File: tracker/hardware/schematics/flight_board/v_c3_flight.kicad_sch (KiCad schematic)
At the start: 28 parts, among them J1 Prog_Header, J2 Debug_Header, U1 ESP32-C3-WROOM-02, U2 LoRa2021_Gen4, U3 MAX-M10S, U4 TPS7A02, U5 MS5611-01BA

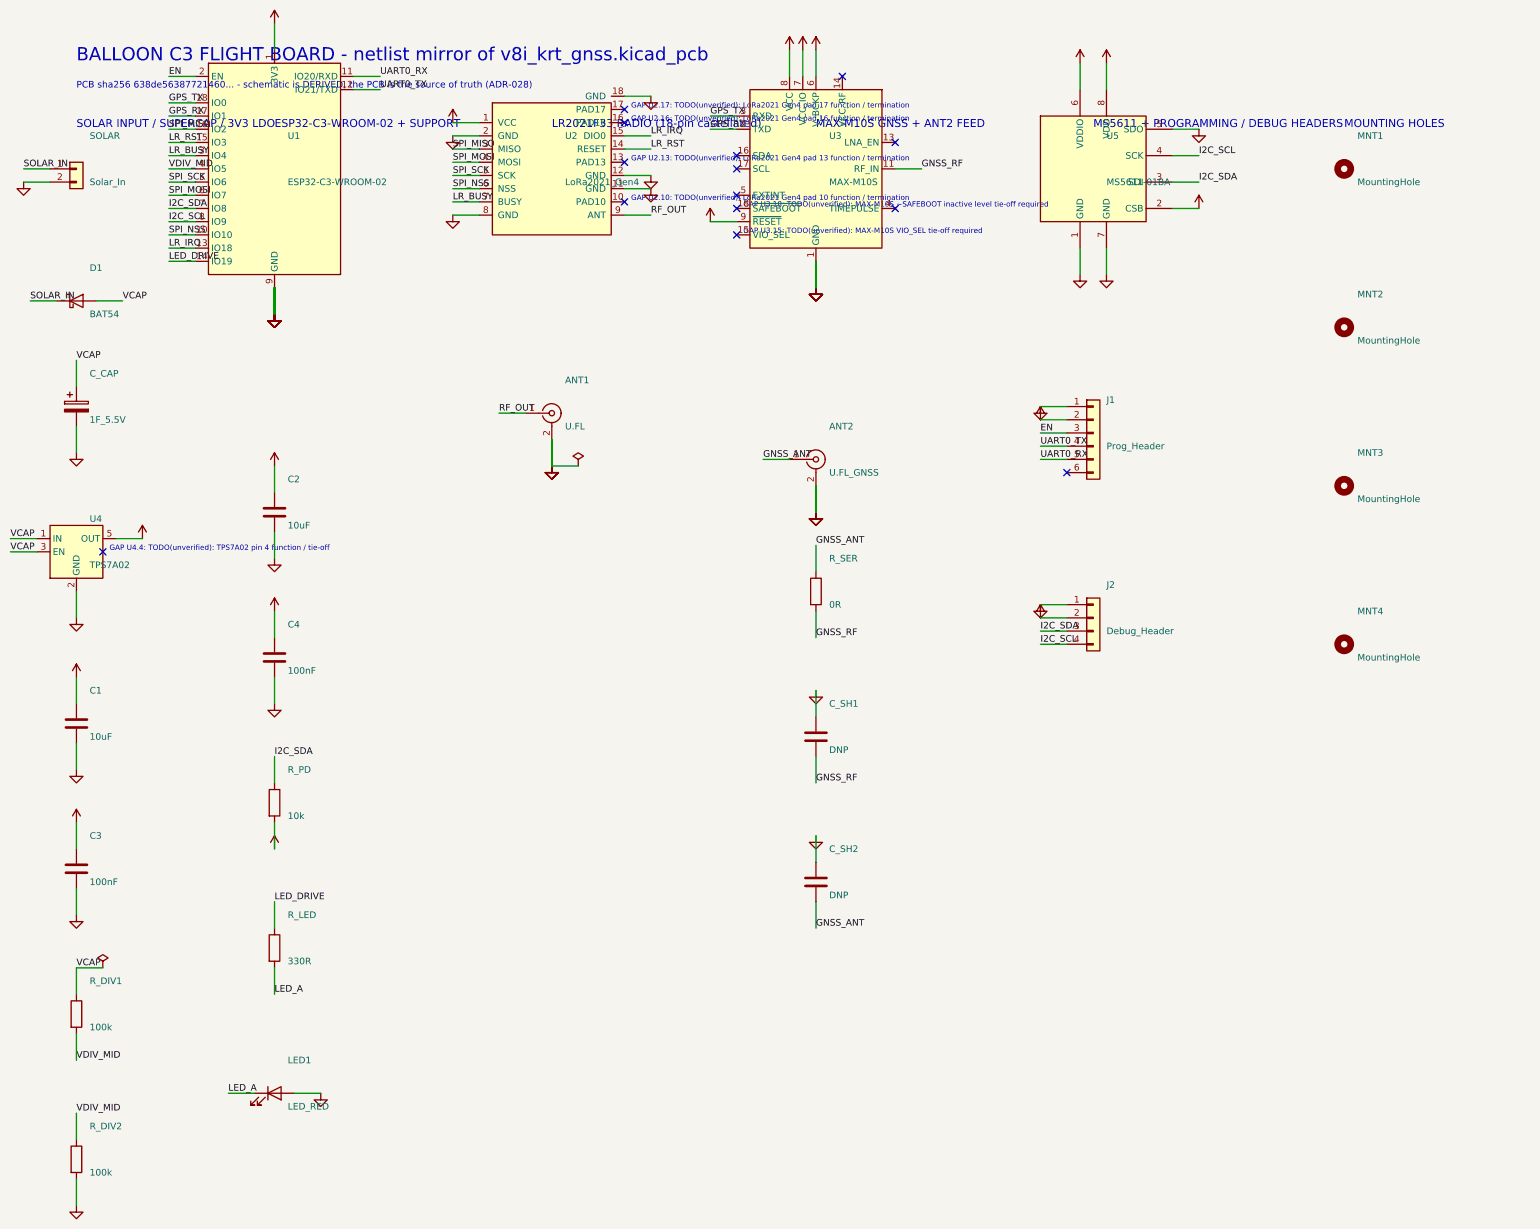
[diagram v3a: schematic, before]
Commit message: fix(sch): resolve 7 floating-pin TODO(unverified) markers from vendor docs
Resolves all 7 netless-pad TODOs on the v8i-derived flight schematic:

- U2.10/13/16/17: LoRa2021 Gen4 module pads renamed to ANT_2G4, VTCXO,
  DIO8, DIO7 and documented with citations from the NiceRF module V1.3
  datasheet and the Semtech LR2021 v2.2 datasheet.
- U3.15 VIO_SEL: leave open for 3.3 V design (u-blox MAX-M10S integration
  manual UBX-20053088 R05, Table 1 and s4.1.2).
- U3.18 SAFEBOOT_N: leave open for normal operation (u-blox MAX-M10S
  integration manual UBX-20053088 R05, Table 1 and s3.2.3.2).
- U4.4 TPS7A02: NC pin, leave floating (TI TPS7A02 datasheet SBVS277C,
  Table 5-1, DBV/SOT-23-5).

Generator: DECLARED_GAP renamed to RESOLVED_NC; check_sch_gates.py GATE 4
updated to match.  No nets were changed; the PCB is still the source of
truth.  Regenerated netlist still has 28 components and ALL GATES PASS.

Refs ADR-BRIEF-6
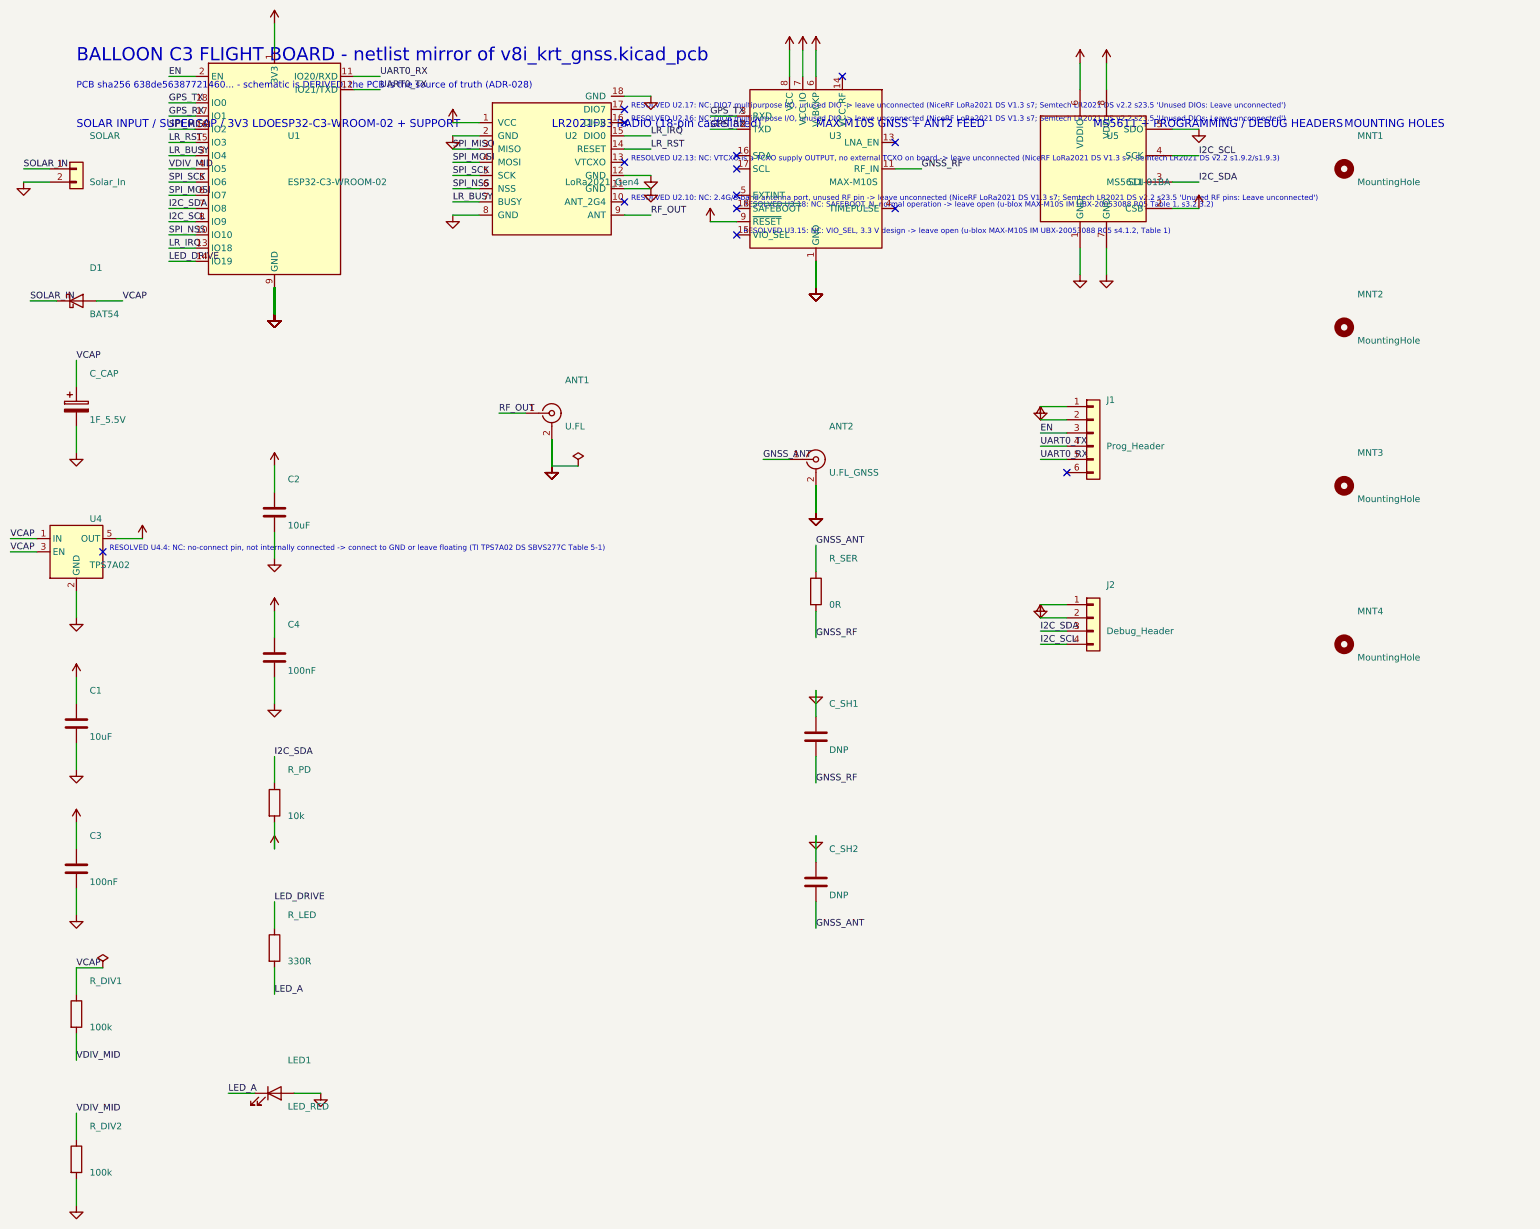
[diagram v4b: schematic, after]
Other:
- note added: "RESOLVED U2.10: NC: 2.4G/S-band antenna port, unused RF pin -> leave unconnected (NiceRF LoRa2021 DS V1.3 s7; Semtech LR2021 DS v2.2 s23.5 'Unused RF pins: Leave unconnected')"
- note added: "RESOLVED U2.13: NC: VTCXO is a TCXO supply OUTPUT, no external TCXO on board -> leave unconnected (NiceRF LoRa2021 DS V1.3 s7; Semtech LR2021 DS v2.2 s1.9.2/s1.9.3)"
- note added: "RESOLVED U2.16: NC: DIO8 multipurpose I/O, unused DIO -> leave unconnected (NiceRF LoRa2021 DS V1.3 s7; Semtech LR2021 DS v2.2 s23.5 'Unused DIOs: Leave unconnected')"
- note added: "RESOLVED U2.17: NC: DIO7 multipurpose I/O, unused DIO -> leave unconnected (NiceRF LoRa2021 DS V1.3 s7; Semtech LR2021 DS v2.2 s23.5 'Unused DIOs: Leave unconnected')"
- note added: "RESOLVED U3.15: NC: VIO_SEL, 3.3 V design -> leave open (u-blox MAX-M10S IM UBX-20053088 R05 s4.1.2, Table 1)"
- note added: "RESOLVED U3.18: NC: SAFEBOOT_N, normal operation -> leave open (u-blox MAX-M10S IM UBX-20053088 R05 Table 1, s3.2.3.2)"
- note added: "RESOLVED U4.4: NC: no-connect pin, not internally connected -> connect to GND or leave floating (TI TPS7A02 DS SBVS277C Table 5-1)"
- note removed: "GAP U2.10: TODO(unverified): LoRa2021 Gen4 pad 10 function / termination"
- note removed: "GAP U2.13: TODO(unverified): LoRa2021 Gen4 pad 13 function / termination"
- note removed: "GAP U2.16: TODO(unverified): LoRa2021 Gen4 pad 16 function / termination"
- note removed: "GAP U2.17: TODO(unverified): LoRa2021 Gen4 pad 17 function / termination"
- note removed: "GAP U3.15: TODO(unverified): MAX-M10S VIO_SEL tie-off required"
- note removed: "GAP U3.18: TODO(unverified): MAX-M10S ~SAFEBOOT inactive level tie-off required"
- note removed: "GAP U4.4: TODO(unverified): TPS7A02 pin 4 function / tie-off"
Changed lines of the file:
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@@
 		(at 152.4 53.34)
 	)
-	(text "GAP U4.4: TODO(unverified): TPS7A02 pin 4 function / tie-off"
+	(text "RESOLVED U4.4: NC: no-connect pin, not internally connected -> connect to GND or leave floating (TI TPS7A02 DS SBVS277C Table 5-1)"
 		(exclude_from_sim no)
 		(at 31.75 119.38 0)
@@
 		)
 	)
-	(text "GAP U2.10: TODO(unverified): LoRa2021 Gen4 pad 10 function / termination"
+	(text "RESOLVED U2.10: NC: 2.4G/S-band antenna port, unused RF pin -> leave unconnected (NiceRF LoRa2021 DS V1.3 s7; Semtech LR2021 DS v2.2 s23.5 'Unused RF pins: Leave unconnected')"
 		(exclude_from_sim no)
 		(at 132.08 52.07 0)
@@
 		)
 	)
-	(text "GAP U2.13: TODO(unverified): LoRa2021 Gen4 pad 13 function / termination"
+	(text "RESOLVED U2.13: NC: VTCXO is a TCXO supply OUTPUT, no external TCXO on board -> leave unconnected (NiceRF LoRa2021 DS V1.3 s7; Semtech LR2021 DS v2.2 s1.9.2/s1.9.3)"
 		(exclude_from_sim no)
 		(at 132.08 44.45 0)
@@
 		)
 	)
-	(text "GAP U2.16: TODO(unverified): LoRa2021 Gen4 pad 16 function / termination"
+	(text "RESOLVED U2.16: NC: DIO8 multipurpose I/O, unused DIO -> leave unconnected (NiceRF LoRa2021 DS V1.3 s7; Semtech LR2021 DS v2.2 s23.5 'Unused DIOs: Leave unconnected')"
 		(exclude_from_sim no)
 		(at 132.08 36.83 0)
@@
 		)
 	)
-	(text "GAP U2.17: TODO(unverified): LoRa2021 Gen4 pad 17 function / termination"
+	(text "RESOLVED U2.17: NC: DIO7 multipurpose I/O, unused DIO -> leave unconnected (NiceRF LoRa2021 DS V1.3 s7; Semtech LR2021 DS v2.2 s23.5 'Unused DIOs: Leave unconnected')"
 		(exclude_from_sim no)
 		(at 132.08 34.29 0)
@@
 		)
 	)
-	(text "GAP U3.15: TODO(unverified): MAX-M10S VIO_SEL tie-off required"
+	(text "RESOLVED U3.15: NC: VIO_SEL, 3.3 V design -> leave open (u-blox MAX-M10S IM UBX-20053088 R05 s4.1.2, Table 1)"
 		(exclude_from_sim no)
 		(at 153.67 58.42 0)
@@
 		)
 	)
-	(text "GAP U3.18: TODO(unverified): MAX-M10S ~SAFEBOOT inactive level tie-off required"
+	(text "RESOLVED U3.18: NC: SAFEBOOT_N, normal operation -> leave open (u-blox MAX-M10S IM UBX-20053088 R05 Table 1, s3.2.3.2)"
 		(exclude_from_sim no)
 		(at 153.67 53.34 0)
